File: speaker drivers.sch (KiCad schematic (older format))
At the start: 21 parts, among them P1 CONN_01X02

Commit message: ENH: Revisions to speaker drivers
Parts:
- removed C1: 33nF, Capacitors_ThroughHole:C_Disc_D6_P5, symbol C-RESCUE-speaker_drivers
- removed C10, CL5: 0.1uF, LBHB:capacitor-2x4mm-L_2.5mm, symbol C-RESCUE-speaker_drivers
- removed C2: 1.2nF, Capacitors_ThroughHole:C_Disc_D6_P5, symbol C-RESCUE-speaker_drivers
- removed C9: 68nF, Capacitors_ThroughHole:C_Disc_D6_P5, symbol C-RESCUE-speaker_drivers
- removed R1: 10k, Discret:R3-5, symbol R-RESCUE-speaker_drivers
- removed R2, R5: 1k, Discret:R3-5, symbol R-RESCUE-speaker_drivers
- removed R3: 49.9, Discret:R3, symbol R-RESCUE-speaker_drivers
- removed R4: 8.2, Discret:R4-5, symbol R-RESCUE-speaker_drivers
- added C1: 10u, LBHB:capacitor-D_5mm-L_2mm, symbol C
- added CB1: 0.1uF, LBHB:capacitor-2x4mm-L_2.5mm, symbol C-RESCUE-speaker_drivers
- added L1: 100u, LBHB:inductor-12mm, symbol L_Small
- added R1, R5: 100k, LBHB:resistor-13x4mm, symbol R
- added R2: 1k, LBHB:resistor-13x4mm, symbol R
- added R3: 10, LBHB:resistor-13x4mm, symbol R
- added R4: 10k, LBHB:resistor-13x4mm, symbol R
- B1, B2: footprint LBHB:BUF634 -> LBHB:BUF634_compact_HeatSink
- renumbered CL6 to CB2, C4 to CB3, C3 to CB4, CL1 to CB5, CL2 to CB6
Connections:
- wire segments 57 -> 45
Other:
- moved on the sheet: CB2, CB5, CB6, P1, V1

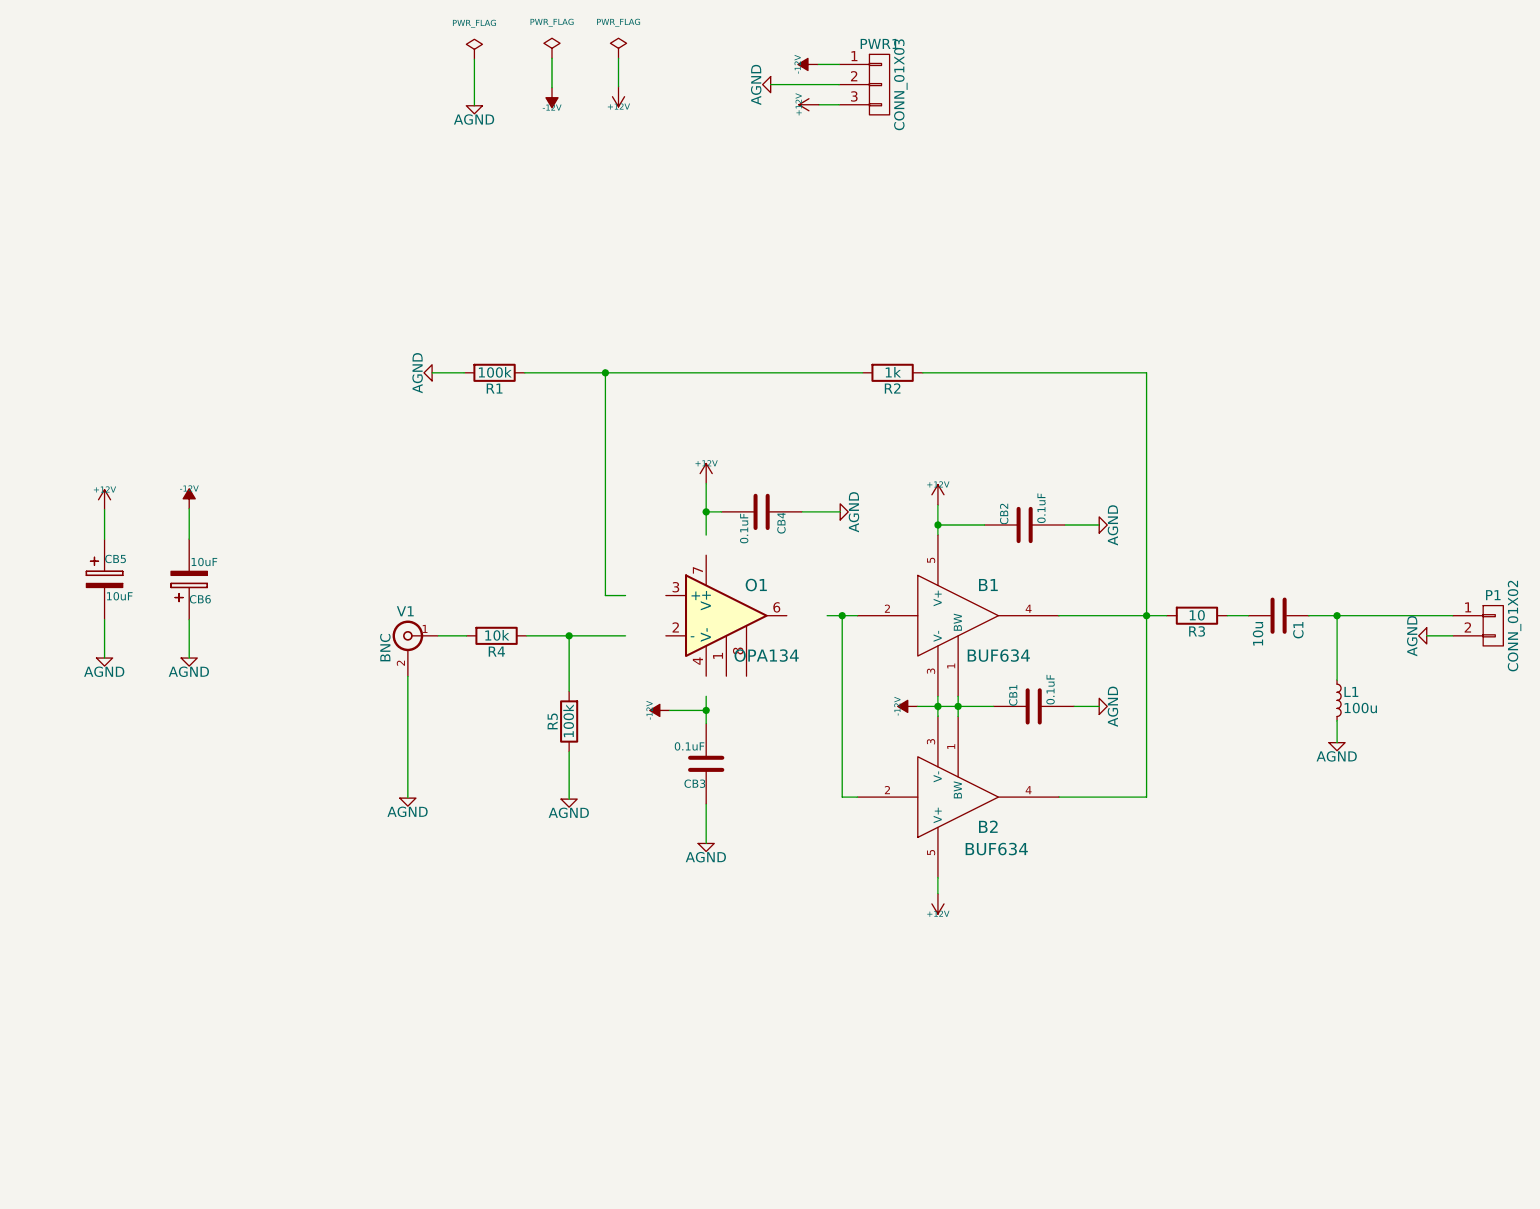
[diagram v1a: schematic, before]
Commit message: Fixed bug in previous version and updated design
* Inverting and noninverting inputs were swapped in the schematic. Fixed
  this bug.
* Removed the highpass filter that follows the current buffer with a
  highpass filter at the input to the current buffer. Highpass filter
  simply removes DC offset now.
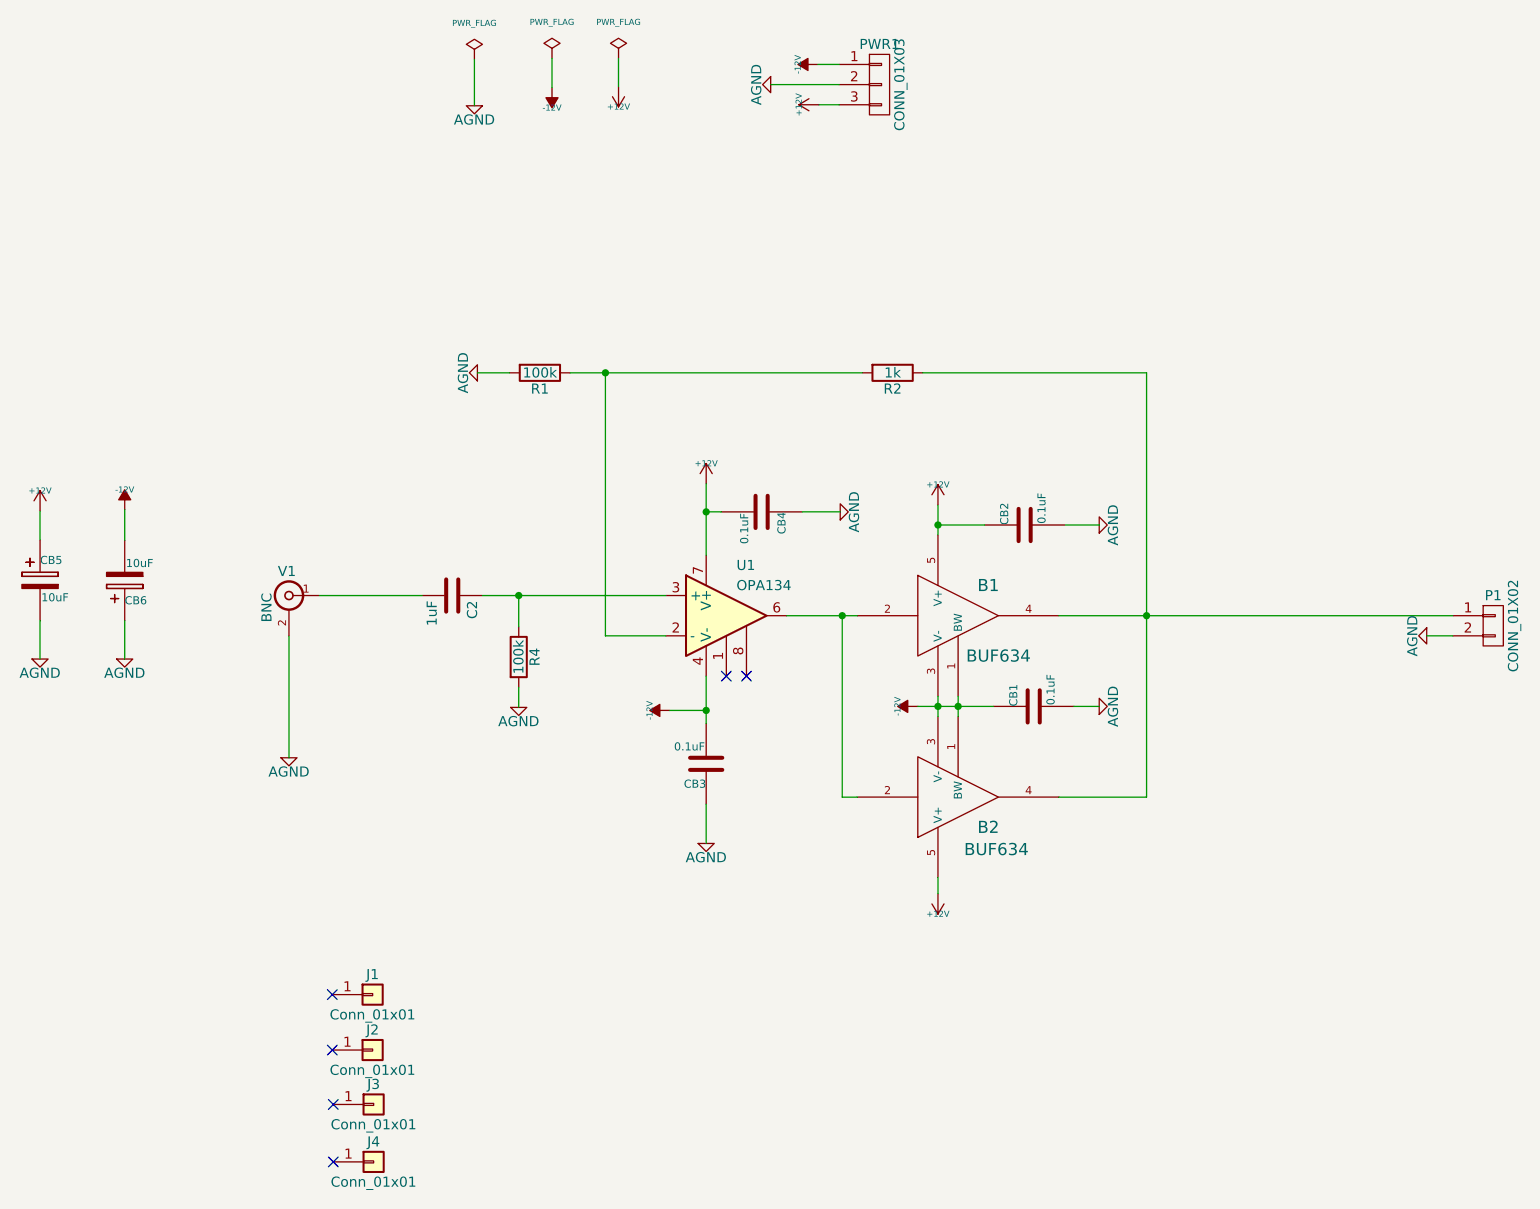
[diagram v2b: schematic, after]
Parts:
- removed C1: 10u, LBHB:capacitor-D_5mm-L_2mm, symbol C
- removed L1: 100u, LBHB:inductor-12mm, symbol L_Small
- removed O1: OPA134, Housings_DIP:DIP-8_W7.62mm_LongPads, symbol OPA134
- removed R3: 10, LBHB:resistor-13x4mm, symbol R
- removed R5: 100k, LBHB:resistor-13x4mm, symbol R
- added C2: 1uF, Capacitor_THT:CP_Radial_D5.0mm_P2.50mm, symbol C
- added J1, J2, J3, J4: Conn_01x01, MountingHole:MountingHole_3.2mm_M3, symbol Conn_01x01
- added U1: OPA134, Housings_DIP:DIP-8_W7.62mm_LongPads, symbol OPA134
- B1, B2: footprint LBHB:BUF634_compact_HeatSink -> TO_SOT_Packages_THT:TO-220-5_Vertical
- CB1, CB2, CB3, CB4: footprint LBHB:capacitor-2x4mm-L_2.5mm -> custom:C_Rect_L4.0mm_W3.5mm_P2.50mm
- CB5, CB6: footprint LBHB:capacitor-D_4mm-L_2.4mm -> Capacitor_THT:CP_Radial_D5.0mm_P2.50mm
- P1: footprint Socket_Strips:Socket_Strip_Straight_1x02 -> Conn_PinHeader_2.54mm:PinHeader_1x02_P2.54mm_Vertical
- PWR1: footprint Socket_Strips:Socket_Strip_Straight_1x03 -> Conn_PinHeader_2.54mm:PinHeader_1x03_P2.54mm_Vertical
- R1, R2: footprint LBHB:resistor-13x4mm -> Resistor_THT:R_Axial_DIN0207_L6.3mm_D2.5mm_P7.62mm_Horizontal
- R4: value 10k -> 100k; footprint LBHB:resistor-13x4mm -> Resistor_THT:R_Axial_DIN0207_L6.3mm_D2.5mm_P7.62mm_Horizontal
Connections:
- wire segments 45 -> 41
- no-connect marks 0 -> 6
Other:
- moved on the sheet: CB5, CB6, R1, V1

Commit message: Added readme
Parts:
- B1, B2: Notes (none) -> heat sink recommended; Part number (none) -> BUF634T
- C2: Notes (none) -> metal film; Part number (none) -> MKS02-1/50/10
- CB1, CB2, CB3, CB4: Part number (none) -> RDER72A104K1S1H03A
- CB5, CB6: Notes (none) -> tantalum recommended; Part number (none) -> TAP106M025SCS
- J1, J2, J3, J4: value Conn_01x01 -> mounting hole
- P1: value CONN_01X02 -> 0.1\" header
- P2: renamed from PWR1; value CONN_01X03 -> 0.1\" header
- P3: renamed from V1; value BNC -> 0.1\" header
- R1, R4: Part number (none) -> YR1B100KCC
- R2: Part number (none) -> YR1B1K0CC
- U1: Part number (none) -> OPA134PA
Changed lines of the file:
@@
 F 2 "TO_SOT_Packages_THT:TO-220-5_Vertical" H 6525 3855 60  0001 C CNN
 F 3 "" H 6525 3855 60  0000 C CNN
+F 4 "BUF634T" H 6525 3855 60  0001 C CNN "Part number"
+F 5 "heat sink recommended" H 6525 3855 60  0001 C CNN "Notes"
 	1    6525 3855
 	1    0    0    -1
@@
 F 2 "Capacitor_THT:CP_Radial_D5.0mm_P2.50mm" H 2008 3530 30  0001 C CNN
 F 3 "" H 1970 3680 60  0000 C CNN
+F 4 "TAP106M025SCS" H 1970 3680 60  0001 C CNN "Part number"
+F 5 "tantalum recommended" H 1970 3680 60  0001 C CNN "Notes"
 	1    1970 3680
 	1    0    0    -1
@@
 F 2 "custom:C_Rect_L4.0mm_W3.5mm_P2.50mm" H 6893 3255 30  0001 C CNN
 F 3 "" H 6855 3405 60  0000 C CNN
+F 4 "RDER72A104K1S1H03A" H 6855 3405 60  0001 C CNN "Part number"
 	1    6855 3405
 	0    -1   -1   0
 $EndComp
 $Comp
-L BNC V1
+L BNC P3
 U 1 1 564F895D
 P 3205 3755
-F 0 "V1" H 3215 3875 50  0000 C CNN
-F 1 "BNC" V 3315 3695 50  0000 C CNN
+F 0 "P3" H 3215 3875 50  0000 C CNN
+F 1 "0.1\" header" V 3315 3695 50  0000 C CNN
 F 2 "Socket_Strips:Socket_Strip_Straight_1x02" H 3205 3755 60  0001 C CNN
 F 3 "" H 3205 3755 60  0000 C CNN
@@
 $EndComp
 $Comp
-L CONN_01X03 PWR1
+L CONN_01X03 P2
 U 1 1 564FBDAF
 P 6135 1220
-F 0 "PWR1" H 6135 1420 50  0000 C CNN
-F 1 "CONN_01X03" V 6235 1220 50  0000 C CNN
+F 0 "P2" H 6135 1420 50  0000 C CNN
+F 1 "0.1\" header" V 6235 1220 50  0000 C CNN
 F 2 "Conn_PinHeader_2.54mm:PinHeader_1x03_P2.54mm_Vertical" H 6135 1220 60  0001 C CNN
 F 3 "" H 6135 1220 60  0000 C CNN
@@
 F 2 "custom:C_Rect_L4.0mm_W3.5mm_P2.50mm" H 5588 3190 30  0001 C CNN
 F 3 "" H 5550 3340 60  0000 C CNN
+F 4 "RDER72A104K1S1H03A" H 5550 3340 60  0001 C CNN "Part number"
 	1    5550 3340
 	0    1    1    0
@@
 F 2 "custom:C_Rect_L4.0mm_W3.5mm_P2.50mm" H 5313 4440 30  0001 C CNN
 F 3 "" H 5275 4590 60  0000 C CNN
+F 4 "RDER72A104K1S1H03A" H 5275 4590 60  0001 C CNN "Part number"
 	1    5275 4590
 	-1   0    0    1
@@
 P 9180 3905
 F 0 "P1" H 9180 4055 50  0000 C CNN
-F 1 "CONN_01X02" V 9280 3905 50  0000 C CNN
+F 1 "0.1\" header" V 9280 3905 50  0000 C CNN
 F 2 "Conn_PinHeader_2.54mm:PinHeader_1x02_P2.54mm_Vertical" H 9180 3905 60  0001 C CNN
 F 3 "" H 9180 3905 60  0000 C CNN
@@
 F 2 "Resistor_THT:R_Axial_DIN0207_L6.3mm_D2.5mm_P7.62mm_Horizontal" V 6130 2650 50  0001 C CNN
 F 3 "" H 6200 2650 50  0000 C CNN
+F 4 "YR1B1K0CC" H 6200 2650 60  0001 C CNN "Part number"
 	1    6200 2650
 	0    1    1    0
@@
 F 2 "Resistor_THT:R_Axial_DIN0207_L6.3mm_D2.5mm_P7.62mm_Horizontal" V 4380 2650 50  0001 C CNN
 F 3 "" H 4450 2650 50  0000 C CNN
+F 4 "YR1B100KCC" H 4450 2650 60  0001 C CNN "Part number"
 	1    4450 2650
 	0    1    1    0
@@
 F 2 "Capacitor_THT:CP_Radial_D5.0mm_P2.50mm" H 2428 3530 30  0001 C CNN
 F 3 "" H 2390 3680 60  0000 C CNN
+F 4 "TAP106M025SCS" H 2390 3680 60  0001 C CNN "Part number"
+F 5 "tantalum recommended" H 2390 3680 60  0001 C CNN "Notes"
 	1    2390 3680
 	1    0    0    1
@@
 F 2 "custom:C_Rect_L4.0mm_W3.5mm_P2.50mm" H 6938 4155 30  0001 C CNN
 F 3 "" H 6900 4305 60  0000 C CNN
+F 4 "RDER72A104K1S1H03A" H 6900 4305 60  0001 C CNN "Part number"
 	1    6900 4305
 	0    -1   -1   0
@@
 F 2 "TO_SOT_Packages_THT:TO-220-5_Vertical" H 6525 4755 60  0001 C CNN
 F 3 "" H 6525 4755 60  0000 C CNN
+F 4 "BUF634T" H 6525 4755 60  0001 C CNN "Part number"
+F 5 "heat sink recommended" H 6525 4755 60  0001 C CNN "Notes"
 	1    6525 4755
 	1    0    0    1
@@
 F 2 "Housings_DIP:DIP-8_W7.62mm_LongPads" H 5425 3905 50  0001 C CNN
 F 3 "" H 5425 4005 50  0001 C CNN
+F 4 "OPA134PA" H 5375 3855 60  0001 C CNN "Part number"
 	1    5375 3855
 	1    0    0    -1
@@
 P 3620 5735
 F 0 "J1" H 3620 5835 50  0000 C CNN
-F 1 "Conn_01x01" H 3620 5635 50  0000 C CNN
+F 1 "mounting hole" H 3620 5635 50  0000 C CNN
 F 2 "MountingHole:MountingHole_3.2mm_M3" H 3620 5735 50  0001 C CNN
 F 3 "" H 3620 5735 50  0001 C CNN
@@
 P 3620 6010
 F 0 "J2" H 3620 6110 50  0000 C CNN
-F 1 "Conn_01x01" H 3620 5910 50  0000 C CNN
+F 1 "mounting hole" H 3620 5910 50  0000 C CNN
 F 2 "MountingHole:MountingHole_3.2mm_M3" H 3620 6010 50  0001 C CNN
 F 3 "" H 3620 6010 50  0001 C CNN
@@
 P 3625 6280
 F 0 "J3" H 3625 6380 50  0000 C CNN
-F 1 "Conn_01x01" H 3625 6180 50  0000 C CNN
+F 1 "mounting hole" H 3625 6180 50  0000 C CNN
 F 2 "MountingHole:MountingHole_3.2mm_M3" H 3625 6280 50  0001 C CNN
 F 3 "" H 3625 6280 50  0001 C CNN
@@
 P 3625 6565
 F 0 "J4" H 3625 6665 50  0000 C CNN
-F 1 "Conn_01x01" H 3625 6465 50  0000 C CNN
+F 1 "mounting hole" H 3625 6465 50  0000 C CNN
 F 2 "MountingHole:MountingHole_3.2mm_M3" H 3625 6565 50  0001 C CNN
 F 3 "" H 3625 6565 50  0001 C CNN
@@
 F 2 "Capacitor_THT:CP_Radial_D5.0mm_P2.50mm" H 4053 3605 50  0001 C CNN
 F 3 "" H 4015 3755 50  0001 C CNN
+F 4 "MKS02-1/50/10" H 4015 3755 60  0001 C CNN "Part number"
+F 5 "metal film" H 4015 3755 60  0001 C CNN "Notes"
 	1    4015 3755
 	0    1    1    0
@@
 F 2 "Resistor_THT:R_Axial_DIN0207_L6.3mm_D2.5mm_P7.62mm_Horizontal" V 4275 4060 50  0001 C CNN
 F 3 "" H 4345 4060 50  0001 C CNN
+F 4 "YR1B100KCC" H 4345 4060 60  0001 C CNN "Part number"
 	1    4345 4060
 	1    0    0    -1
